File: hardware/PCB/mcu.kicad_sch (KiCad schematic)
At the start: 42 parts, among them J2 Conn_02x05_Odd_Even, J3 USB_C_Receptacle_USB2.0_16P, SW1 RESET, SW2 PROG, U4 32 MHz, U5 USBLC6-2, Y1 Crystal

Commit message: Update mcu.kicad_sch
schematic almost ready
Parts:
- removed J3: USB_C_Receptacle_USB2.0_16P, symbol Connector:USB_C_Receptacle_USB2.0_16P
- removed R14, R15: 10k, symbol Device:R_US
- removed R16, R17: 5.1k, symbol Device:R_US
- added J10, J11, J5, J6, J7, J8, J9: Conn_01x03, symbol Connector_Generic:Conn_01x03
- added J12: USB_C_Receptacle_USB2.0_16P, symbol Connector:USB_C_Receptacle_USB2.0_16P
- added R20, R21, R22, R23, R24, R25, R56, R57, R58: 10k, symbol Device:R_US
- added R53: 4.7k, symbol Device:R_US
- added R54, R55: 5.1k, symbol Device:R_US
- C10, C11, C12, C13, C14, C15, C16, C17, C18, C19, C20, C21, C22, C23, C24, C25, C26, C27, C31, C49, C8: footprint (none) -> Capacitor_SMD:C_0603_1608Metric
- C30: footprint (none) -> Capacitor_SMD:C_0201_0603Metric
- C43, C46, C5, C50, C51, C6, C7, C9: footprint (none) -> Capacitor_SMD:C_0805_2012Metric
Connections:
- net +3.3V: now also J10.1 (Pin_1), J11.1 (Pin_1), J5.1 (Pin_1), J6.1 (Pin_1), J7.1 (Pin_1), J9.1 (Pin_1), R57.1
- net BL_DIM: now also U?.87 (PB14)
- net GND: now also J10.2 (Pin_2), J11.2 (Pin_2), J12.A1 (GND), J12.A12 (GND), J12.B1 (GND), J12.B12 (GND), J12.S1 (SHIELD), J5.2 (Pin_2), J6.2 (Pin_2), J7.2 (Pin_2), J8.3 (Pin_3), J9.2 (Pin_2), R20.2, R21.2, R22.2, R23.2, R24.2, R25.2, R54.1, R55.2, R56.2, R58.2
- net LCD_DISP: now also U?.41 (PA0)
- net PROG: now also R58.1
- net RESET: now also R57.2
- net TS_INT: now also U?.20 (PF2)
- net TS_NRST: now also U?.22 (PF4)
- net TS_SCL: now also U?.19 (PF1)
- net TS_SDA: now also U?.18 (PF0)
- net USB_DM: now also J12.A7 (D-), J12.B7 (D-)
- net USB_DP: now also J12.A6 (D+), J12.B6 (D+)
- net VBUS: now also J12.A4 (VBUS), J12.A9 (VBUS), J12.B4 (VBUS), J12.B9 (VBUS), R53.1; no longer U?.128 (PA9)
- net UART6_RX: now reaches U?.153 (PG9)
- net UART6_RX: now also J8.2 (Pin_2)
- net UART6_TX: now reaches U?.158 (PG14)
- net UART6_TX: now also J8.1 (Pin_1)
- net TURNTABLE_SW: now reaches U?.162 (PB3)
- net TURNTABLE_SW: now also J11.3 (Pin_3), R20.1
- net GANTRY_SW: now reaches U?.163 (PB4)
- net GANTRY_SW: now also J5.3 (Pin_3), R21.1
- net EXTRUDER_SW: now reaches U?.164 (PB5)
- net EXTRUDER_SW: now also J6.3 (Pin_3), R22.1
- net REVOLUTE_SW: now reaches U?.165 (PB6)
- net REVOLUTE_SW: now also J7.3 (Pin_3), R23.1
- net DOOR_SW: now reaches U?.166 (PB7)
- net DOOR_SW: now also J9.3 (Pin_3), R24.1
- net TURNTABLE_DIR: now reaches U?.59 (PF12)
- net EXTRUDER_DIR: now reaches U?.60 (PF13)
- net GANTRY_DIR: now reaches U?.61 (PF14)
- net REVOLUTE_DIR: now reaches U?.62 (PF15)
- net TURNTABLE_FLT: now reaches U?.67 (PE7)
- net EXTRUDER_FLT: now reaches U?.68 (PE8)
- net GANTRY_FLT: now reaches U?.69 (PE9)
- net REVOLUTE_FLT: now reaches U?.72 (PE10)
- net AUX_SW: now reaches U?.85 (PB12)
- net AUX_SW: now also J10.3 (Pin_3), R25.1
- net TURNTABLE_STEP: now reaches U?.95 (PD12)
- net EXTRUDER_STEP: now reaches U?.96 (PD13)
- net GANTRY_STEP: now reaches U?.97 (PD14)
- net REVOLUTE_STEP: now reaches U?.98 (PD15)
- new net: R53.2, R56.1, U?.128 (PA9)
- new net: J12.B5 (CC2), R54.2
- new net: J12.A5 (CC1), R55.1
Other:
- note added: "I2C 2"
- note added: "Timer 12 Channel 1"
- note added: "Timer 4 Channel 1"
- note added: "Timer 4 Channel 2"
- note added: "Timer 4 Channel 3"
- note added: "Timer 4 Channel 4"
- note added: "To MOTOR CONTROL"
- note removed: "all unconnected"
- note removed: "leaving disp unconnected until we decide gpio"
- moved on the sheet: C30, C31, C5, C6, C7, C8, J2, SW1, SW2, U4, U5, U?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

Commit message: Filling in more MCU details
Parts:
- C30: footprint Capacitor_SMD:C_0201_0603Metric -> Capacitor_SMD:C_0603_1608Metric
- J10, J11, J5, J6, J7, J9: footprint (none) -> Connector_Molex:Molex_KK-254_AE-6410-03A_1x03_P2.54mm_Vertical; MANUFACTURER (none) -> Molex; Manufacturer_Part_Number (none) -> 0022232031
- J12: footprint (none) -> Connector_USB:USB_C_Receptacle_GCT_USB4105-xx-A_16P_TopMnt_Horizontal; MANUFACTURER (none) -> GCT; Manufacturer_Part_Number (none) -> USB-4105-GF-A
- J2: footprint (none) -> Connector_IDC:IDC-Header_2x05_P2.54mm_Vertical; MANUFACTURER (none) -> Wurth; Manufacturer_Part_Number (none) -> 61201021621
- J8: footprint (none) -> Connector_PinHeader_2.54mm:PinHeader_1x03_P2.54mm_Vertical
- R20, R21, R22, R23, R24, R25, R53, R54, R55, R56, R57, R58: footprint (none) -> Resistor_SMD:R_0805_2012Metric
- U4: MANUFACTURER (none) -> ECS; Manufacturer_Part_Number (none) -> ECS-3225MLVC
- U5: MANUFACTURER (none) -> STMicroelectronics; Manufacturer_Part_Number (none) -> USBLC6-2
- U?: MANUFACTURER (none) -> STMicroelectronic; Manufacturer_Part_Number (none) -> STM32H747IIT
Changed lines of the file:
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@@
 			)
 		)
-		(property "Footprint" ""
+		(property "Footprint" "Connector_Molex:Molex_KK-254_AE-6410-03A_1x03_P2.54mm_Vertical"
 			(at 356.87 48.26 0)
 			(effects
@@
 			)
 		)
+		(property "MANUFACTURER" "Molex"
+			(at 356.87 48.26 0)
+			(effects
+				(font
+					(size 1.27 1.27)
+				)
+			)
+		)
+		(property "Manufacturer_Part_Number" "0022232031"
+			(at 356.87 48.26 0)
+			(effects
+				(font
+					(size 1.27 1.27)
+				)
+			)
+		)
 		(pin "3"
 		)
@@
 			)
 		)
-		(property "Footprint" ""
+		(property "Footprint" "Resistor_SMD:R_0805_2012Metric"
 			(at 37.846 179.324 90)
 			(effects
@@
 			)
 		)
+		(property "MANUFACTURER" "STMicroelectronic"
+			(at 198.12 138.43 0)
+			(effects
+				(font
+					(size 1.27 1.27)
+				)
+			)
+		)
+		(property "Manufacturer_Part_Number" "STM32H747IIT"
+			(at 198.12 138.43 0)
+			(effects
+				(font
+					(size 1.27 1.27)
+				)
+			)
+		)
 		(pin "33"
 		)
@@
 			)
 		)
-		(property "Footprint" ""
+		(property "Footprint" "Connector_Molex:Molex_KK-254_AE-6410-03A_1x03_P2.54mm_Vertical"
 			(at 356.87 22.86 0)
 			(effects
@@
 			)
 		)
+		(property "MANUFACTURER" "Molex"
+			(at 356.87 22.86 0)
+			(effects
+				(font
+					(size 1.27 1.27)
+				)
+			)
+		)
+		(property "Manufacturer_Part_Number" "0022232031"
+			(at 356.87 22.86 0)
+			(effects
+				(font
+					(size 1.27 1.27)
+				)
+			)
+		)
 		(pin "3"
 		)
@@
 			)
 		)
-		(property "Footprint" ""
+		(property "Footprint" "Connector_Molex:Molex_KK-254_AE-6410-03A_1x03_P2.54mm_Vertical"
 			(at 356.87 148.59 0)
 			(effects
@@
 			)
 		)
+		(property "MANUFACTURER" "Molex"
+			(at 356.87 148.59 0)
+			(effects
+				(font
+					(size 1.27 1.27)
+				)
+			)
+		)
+		(property "Manufacturer_Part_Number" "0022232031"
+			(at 356.87 148.59 0)
+			(effects
+				(font
+					(size 1.27 1.27)
+				)
+			)
+		)
 		(pin "3"
 		)
@@
 			)
 		)
-		(property "Footprint" ""
+		(property "Footprint" "Resistor_SMD:R_0805_2012Metric"
 			(at 270.256 73.914 90)
 			(effects
@@
 			)
 		)
+		(property "MANUFACTURER" "ECS"
+			(at 39.37 111.76 0)
+			(effects
+				(font
+					(size 1.27 1.27)
+				)
+			)
+		)
+		(property "Manufacturer_Part_Number" "ECS-3225MLVC"
+			(at 39.37 111.76 0)
+			(effects
+				(font
+					(size 1.27 1.27)
+				)
+			)
+		)
 		(pin "4"
 		)
@@
 			)
 		)
-		(property "Footprint" ""
+		(property "Footprint" "Resistor_SMD:R_0805_2012Metric"
 			(at 350.266 192.786 90)
 			(effects
@@
 			)
 		)
-		(property "Footprint" ""
+		(property "Footprint" "Resistor_SMD:R_0805_2012Metric"
 			(at 350.774 131.064 90)
 			(effects
@@
 			)
 		)
-		(property "Footprint" ""
+		(property "Footprint" "Resistor_SMD:R_0805_2012Metric"
 			(at 350.774 29.464 90)
 			(effects
@@
 			)
 		)
-		(property "Footprint" ""
+		(property "Footprint" "Connector_IDC:IDC-Header_2x05_P2.54mm_Vertical"
 			(at 276.86 251.46 0)
 			(effects
@@
 			)
 		)
+		(property "MANUFACTURER" "Wurth"
+			(at 276.86 251.46 0)
+			(effects
+				(font
+					(size 1.27 1.27)
+				)
+			)
+		)
+		(property "Manufacturer_Part_Number" "61201021621"
+			(at 276.86 251.46 0)
+			(effects
+				(font
+					(size 1.27 1.27)
+				)
+			)
+		)
 		(pin "1"
 		)
@@
 			)
 		)
-		(property "Footprint" ""
+		(property "Footprint" "Resistor_SMD:R_0805_2012Metric"
 			(at 350.774 188.214 90)
 			(effects
@@
 			)
 		)
-		(property "Footprint" ""
+		(property "Footprint" "Resistor_SMD:R_0805_2012Metric"
 			(at 270.256 66.294 90)
 			(effects
@@
 			)
 		)
-		(property "Footprint" "Capacitor_SMD:C_0201_0603Metric"
+		(property "Footprint" "Capacitor_SMD:C_0603_1608Metric"
 			(at 39.37 138.1252 0)
 			(effects
@@
 			)
 		)
-		(property "Footprint" ""
+		(property "Footprint" "Resistor_SMD:R_0805_2012Metric"
 			(at 350.774 54.864 90)
 			(effects
@@
 			)
 		)
-		(property "Footprint" ""
+		(property "Footprint" "Resistor_SMD:R_0805_2012Metric"
 			(at 35.814 212.344 90)
 			(effects
@@
 			)
 		)
+		(property "MANUFACTURER" "STMicroelectronics"
+			(at 388.62 201.93 0)
+			(effects
+				(font
+					(size 1.27 1.27)
+				)
+			)
+		)
+		(property "Manufacturer_Part_Number" "USBLC6-2"
+			(at 388.62 201.93 0)
+			(effects
+				(font
+					(size 1.27 1.27)
+				)
+			)
+		)
 		(pin "2"
 		)
@@
 			)
 		)
-		(property "Footprint" ""
+		(property "Footprint" "Connector_USB:USB_C_Receptacle_GCT_USB4105-xx-A_16P_TopMnt_Horizontal"
 			(at 330.2 199.39 0)
 			(effects
@@
 			)
 		)
+		(property "MANUFACTURER" "GCT"
+			(at 326.39 199.39 0)
+			(effects
+				(font
+					(size 1.27 1.27)
+				)
+			)
+		)
+		(property "Manufacturer_Part_Number" "USB-4105-GF-A"
+			(at 326.39 199.39 0)
+			(effects
+				(font
+					(size 1.27 1.27)
+				)
+			)
+		)
 		(pin "A6"
 		)
@@
 			)
 		)
-		(property "Footprint" ""
+		(property "Footprint" "Resistor_SMD:R_0805_2012Metric"
 			(at 350.774 155.194 90)
 			(effects
@@
 			)
 		)
-		(property "Footprint" ""
+		(property "Footprint" "Connector_Molex:Molex_KK-254_AE-6410-03A_1x03_P2.54mm_Vertical"
 			(at 356.87 124.46 0)
 			(effects
@@
 			)
 		)
+		(property "MANUFACTURER" "Molex"
+			(at 356.87 124.46 0)
+			(effects
+				(font
+					(size 1.27 1.27)
+				)
+			)
+		)
+		(property "Manufacturer_Part_Number" "0022232031"
+			(at 356.87 124.46 0)
+			(effects
+				(font
+					(size 1.27 1.27)
+				)
+			)
+		)
 		(pin "3"
 		)
@@
 			)
 		)
-		(property "Footprint" ""
+		(property "Footprint" "Resistor_SMD:R_0805_2012Metric"
 			(at 350.774 80.264 90)
 			(effects
@@
 			)
 		)
-		(property "Footprint" ""
+		(property "Footprint" "Resistor_SMD:R_0805_2012Metric"
 			(at 350.774 105.664 90)
 			(effects
@@
 			)
 		)
-		(property "Footprint" ""
+		(property "Footprint" "Connector_Molex:Molex_KK-254_AE-6410-03A_1x03_P2.54mm_Vertical"
 			(at 356.87 99.06 0)
 			(effects
@@
 			)
 		)
+		(property "MANUFACTURER" "Molex"
+			(at 356.87 99.06 0)
+			(effects
+				(font
+					(size 1.27 1.27)
+				)
+			)
+		)
+		(property "Manufacturer_Part_Number" "0022232031"
+			(at 356.87 99.06 0)
+			(effects
+				(font
+					(size 1.27 1.27)
+				)
+			)
+		)
 		(pin "3"
 		)
@@
 			)
 		)
-		(property "Footprint" ""
+		(property "Footprint" "Connector_PinHeader_2.54mm:PinHeader_1x03_P2.54mm_Vertical"
 			(at 313.69 147.32 0)
 			(effects
@@
 			)
 		)
-		(property "Footprint" ""
+		(property "Footprint" "Connector_Molex:Molex_KK-254_AE-6410-03A_1x03_P2.54mm_Vertical"
 			(at 356.87 73.66 0)
 			(effects
@@
 			)
 		)
+		(property "MANUFACTURER" "Molex"
+			(at 356.87 73.66 0)
+			(effects
+				(font
+					(size 1.27 1.27)
+				)
+			)
+		)
+		(property "Manufacturer_Part_Number" "0022232031"
+			(at 356.87 73.66 0)
+			(effects
+				(font
+					(size 1.27 1.27)
+				)
+			)
+		)

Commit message: Add footprint for switch and wrap up footprint assignments for MCU
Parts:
- added J13: Conn_01x03, Connector_PinHeader_2.54mm:PinHeader_1x03_P2.54mm_Vertical, symbol Connector_Generic:Conn_01x03
- SW1, SW2: footprint (none) -> CustomFootprints:pts526_1.5mm_gullwing; MANUFACTURER (none) -> C&K; Manufacturer_Part_Number (none) -> PTS526SM15SMTR2 LFS
- Y1: footprint (none) -> Crystal:Crystal_SMD_EuroQuartz_EQ161-2Pin_3.2x1.5mm; MANUFACTURER (none) -> Abracon; Manufacturer_Part_Number (none) -> ABS07-32.768KHZ-T
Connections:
- net EXTRUDER_DIR: now also U?.111 (PG3); no longer U?.60 (PF13)
- net GANTRY_DIR: now also U?.114 (PG4); no longer U?.61 (PF14)
- net GND: now also J13.3 (Pin_3)
- net REVOLUTE_DIR: now also U?.115 (PG5); no longer U?.62 (PF15)
- net SD_CD: now also U?.144 (PD1)
- net TURNTABLE_DIR: now also U?.110 (PG2); no longer U?.59 (PF12)
- new net AUX_SCL: J13.1 (Pin_1), U?.61 (PF14)
- new net AUX_SDA: J13.2 (Pin_2), U?.62 (PF15)
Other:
- note added: "I2C2"
- note added: "I2C4"
- note added: "Programmer header"
- note removed: "CD unconnected"
- note removed: "I2C 2"
- note removed: "Progrommer header"
- note removed: "test point/header for analog pins"
- moved on the sheet: J10, J8, R25

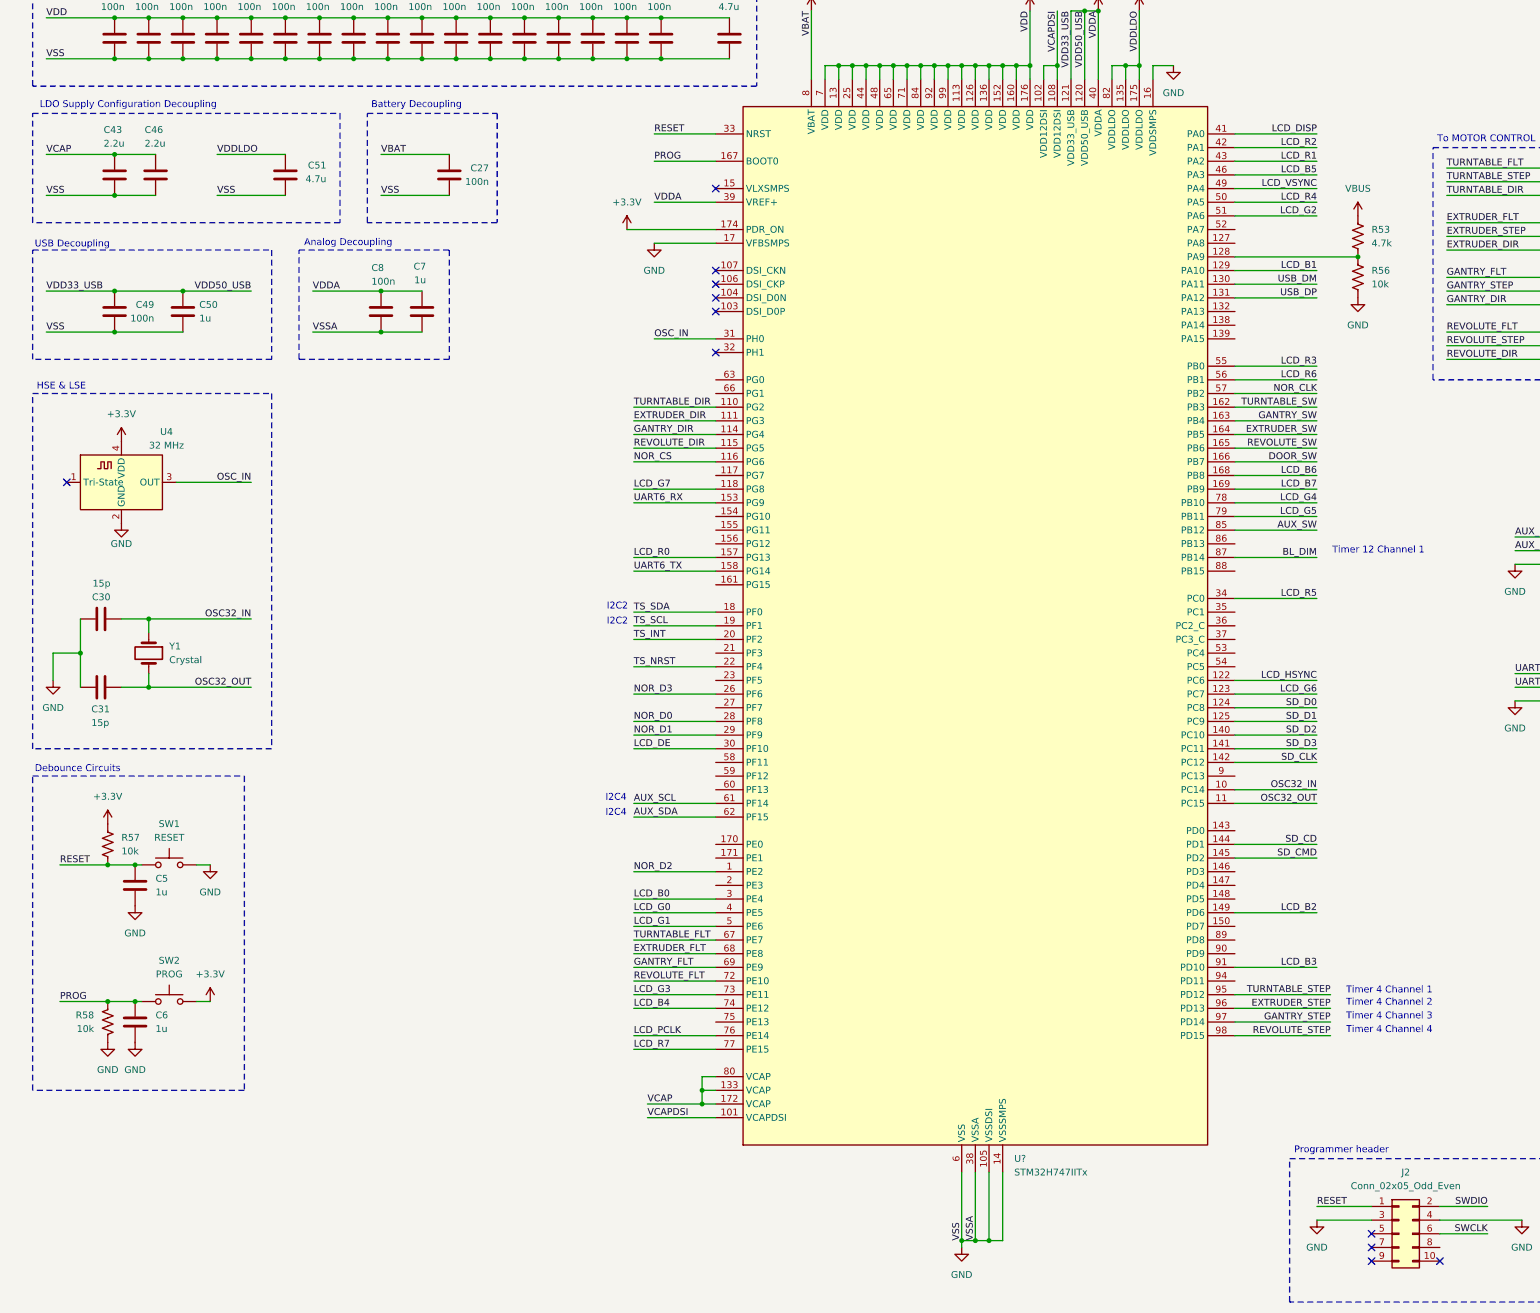
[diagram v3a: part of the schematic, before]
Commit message: MCU schematic: add debugging LEDs and no-connects
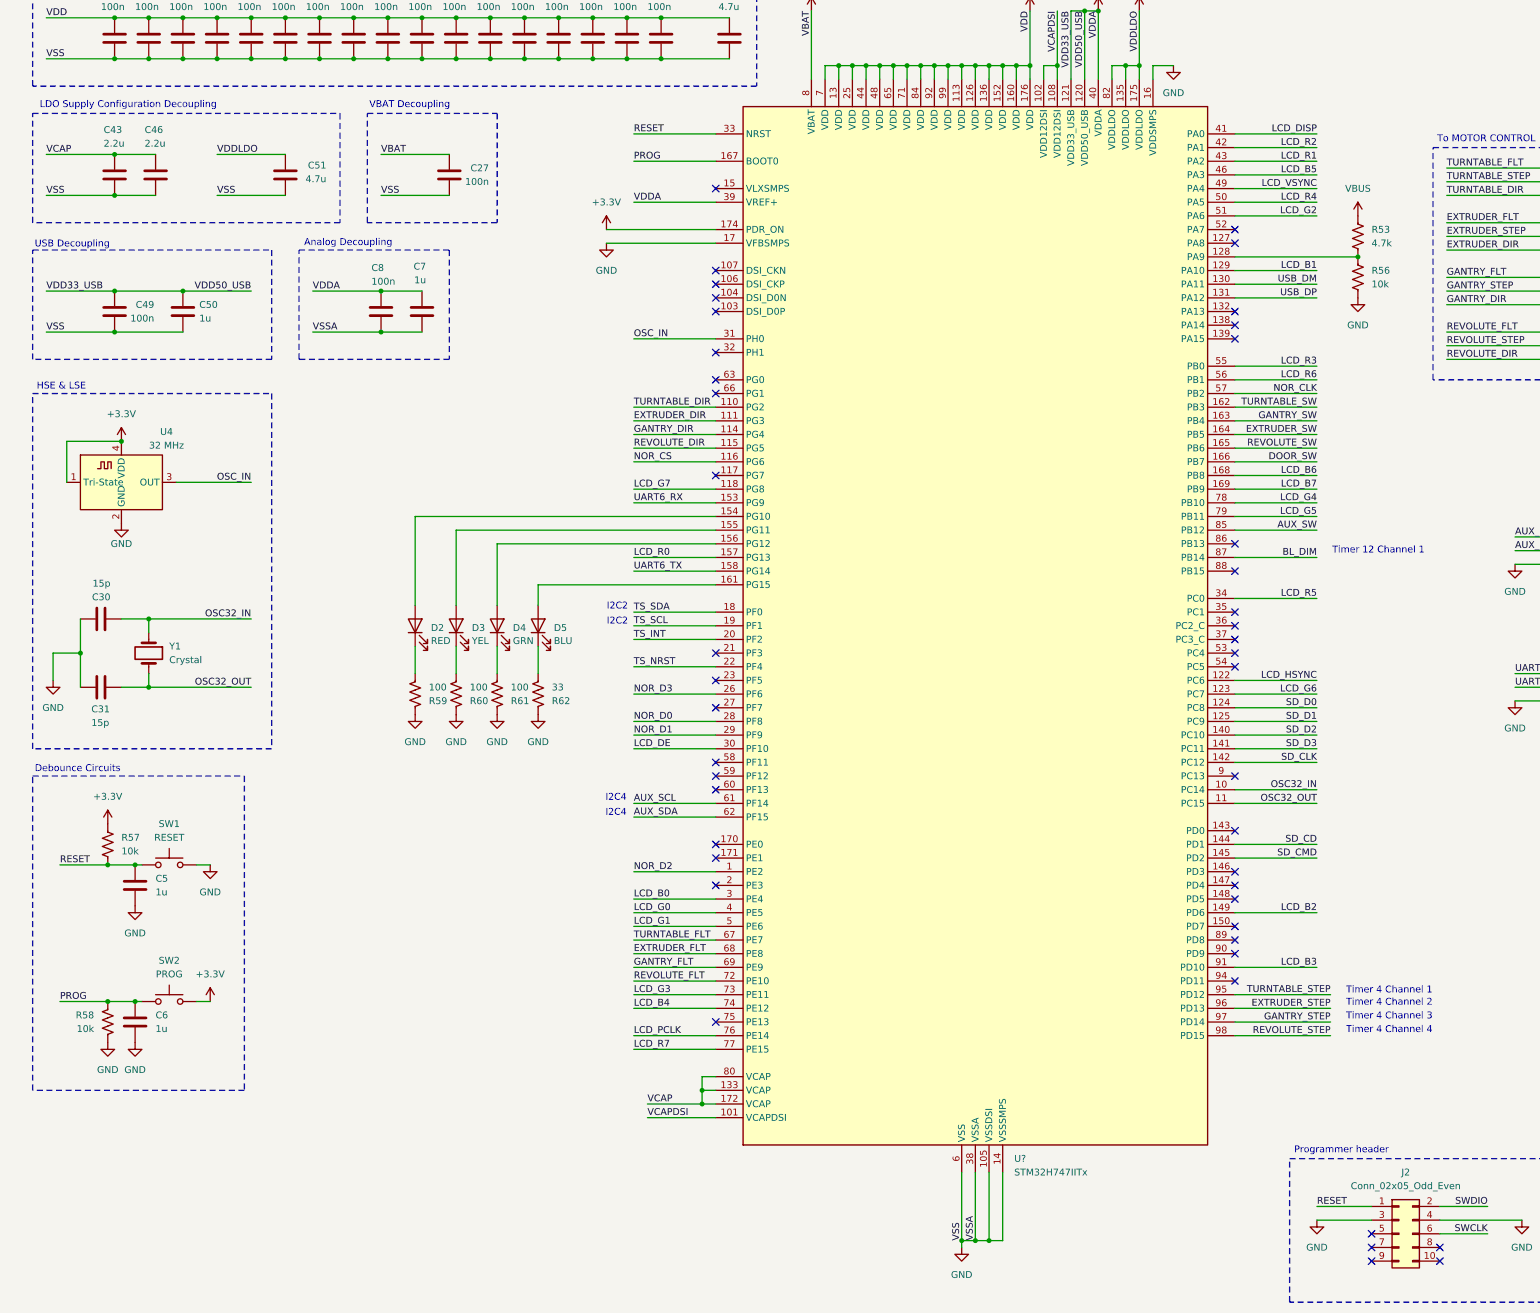
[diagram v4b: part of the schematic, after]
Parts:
- added D2: RED, LED_SMD:LED_0805_2012Metric, symbol Device:LED
- added D3: YEL, LED_SMD:LED_0805_2012Metric, symbol Device:LED
- added D4: GRN, LED_SMD:LED_0805_2012Metric, symbol Device:LED
- added D5: BLU, LED_SMD:LED_0805_2012Metric, symbol Device:LED
- added R59, R60, R61: 100, Resistor_SMD:R_0805_2012Metric, symbol Device:R_US
- added R62: 33, Resistor_SMD:R_0805_2012Metric, symbol Device:R_US
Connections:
- net +3.3V: now also U4.1 (Tri-State)
- net GND: now also R59.1, R60.1, R61.1, R62.1
- net at U?.154 (PG10): now also D2.2 (A)
- net at U?.155 (PG11): now also D3.2 (A)
- net at U?.156 (PG12): now also D4.2 (A)
- net at U?.161 (PG15): now also D5.2 (A)
- new net: D3.1 (K), R60.2
- new net: D5.1 (K), R62.2
- new net: D4.1 (K), R61.2
- new net: D2.1 (K), R59.2
- no-connect marks 13 -> 47
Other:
- note added: "VBAT Decoupling"
- note removed: "Battery Decoupling"

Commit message: Update mcu.kicad_sch
test points
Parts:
- added D6: D, Diode_SMD:D_SOD-323, symbol Device:D
- added R63: 1M, Resistor_SMD:R_0805_2012Metric, symbol Device:R_US
- added TP26, TP27, TP28, TP29: TestPoint, TestPoint:TestPoint_Pad_D1.5mm, symbol Connector:TestPoint
- added TP31: TestPoint, TestPoint:TestPoint_Loop_D2.54mm_Drill1.5mm_Beaded, symbol Connector:TestPoint
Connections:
- net GND: now also R63.1, TP31.1; no longer J12.S1 (SHIELD)
- net OSC32_IN: now also TP26.1
- net OSC32_OUT: now also TP27.1
- net SWCLK: now also TP29.1
- net SWDIO: now also TP28.1
- net VBUS: now also D6.1 (K); no longer J12.A4 (VBUS), J12.A9 (VBUS), J12.B4 (VBUS), J12.B9 (VBUS)
- net CUTTER_EN: now reaches U?.66 (PG1)
- new net: D6.2 (A), J12.A4 (VBUS), J12.A9 (VBUS), J12.B4 (VBUS), J12.B9 (VBUS)
- new net: J12.S1 (SHIELD), R63.2
- no-connect marks 47 -> 46
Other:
- note added: "need decoupling cap"
- moved on the sheet: J10, J11, J12, J13, J5, J6, J7, J8, J9, R20, R21, R22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
